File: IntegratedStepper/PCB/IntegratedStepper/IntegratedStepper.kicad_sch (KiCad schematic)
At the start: 0 parts

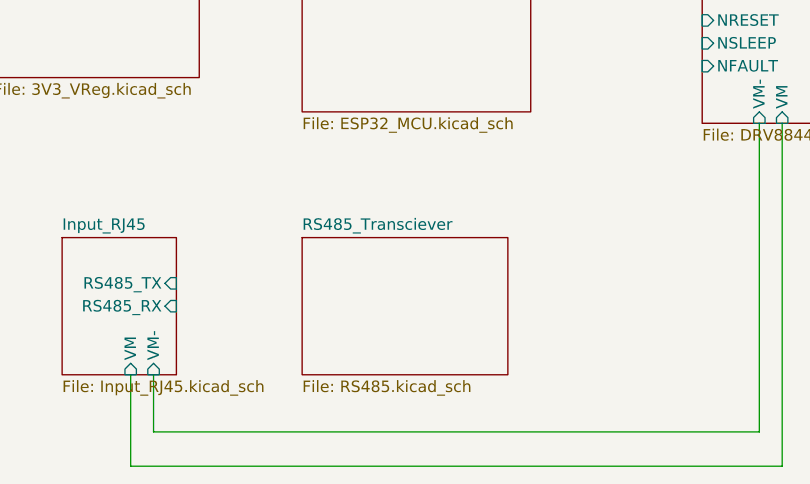
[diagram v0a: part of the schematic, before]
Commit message: Add CAN circuit and edit bus from RS485 to CAN
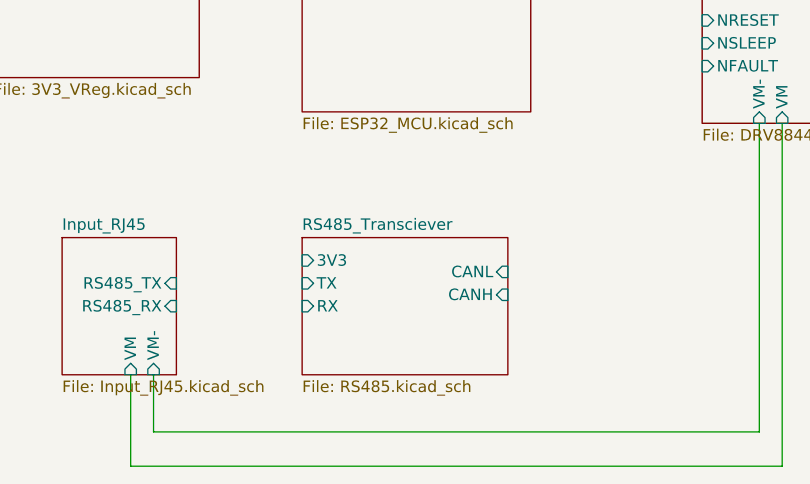
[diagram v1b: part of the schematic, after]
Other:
- sheet RS485_Transciever ports: added 3V3, CANH, CANL, RX, TX; removed none
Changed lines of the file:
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@@
       (effects (font (size 1.27 1.27)) (justify left top))
+    )
+    (pin "TX" input (at 104.14 111.76 180)
+      (effects (font (size 1.27 1.27)) (justify left))
+    )
+    (pin "RX" input (at 104.14 114.3 180)
+      (effects (font (size 1.27 1.27)) (justify left))
+    )
+    (pin "3V3" input (at 104.14 109.22 180)
+      (effects (font (size 1.27 1.27)) (justify left))
+    )
+    (pin "CANL" input (at 127 110.49 0)
+      (effects (font (size 1.27 1.27)) (justify right))
+    )
+    (pin "CANH" input (at 127 113.03 0)
+      (effects (font (size 1.27 1.27)) (justify right))
     )
     (instances

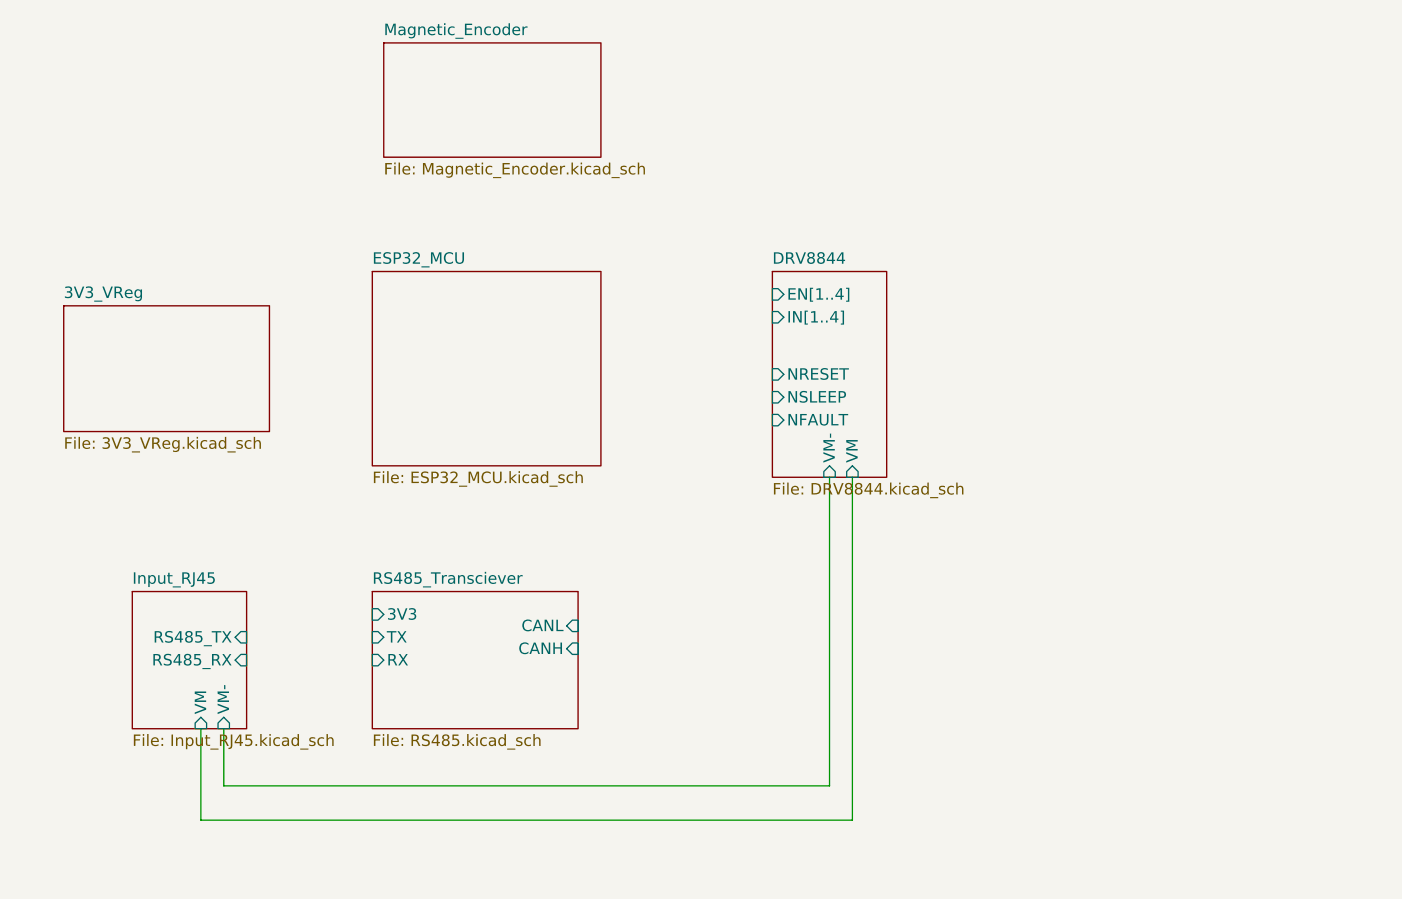
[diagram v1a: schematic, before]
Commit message: update Vreg for Integrated Stepper
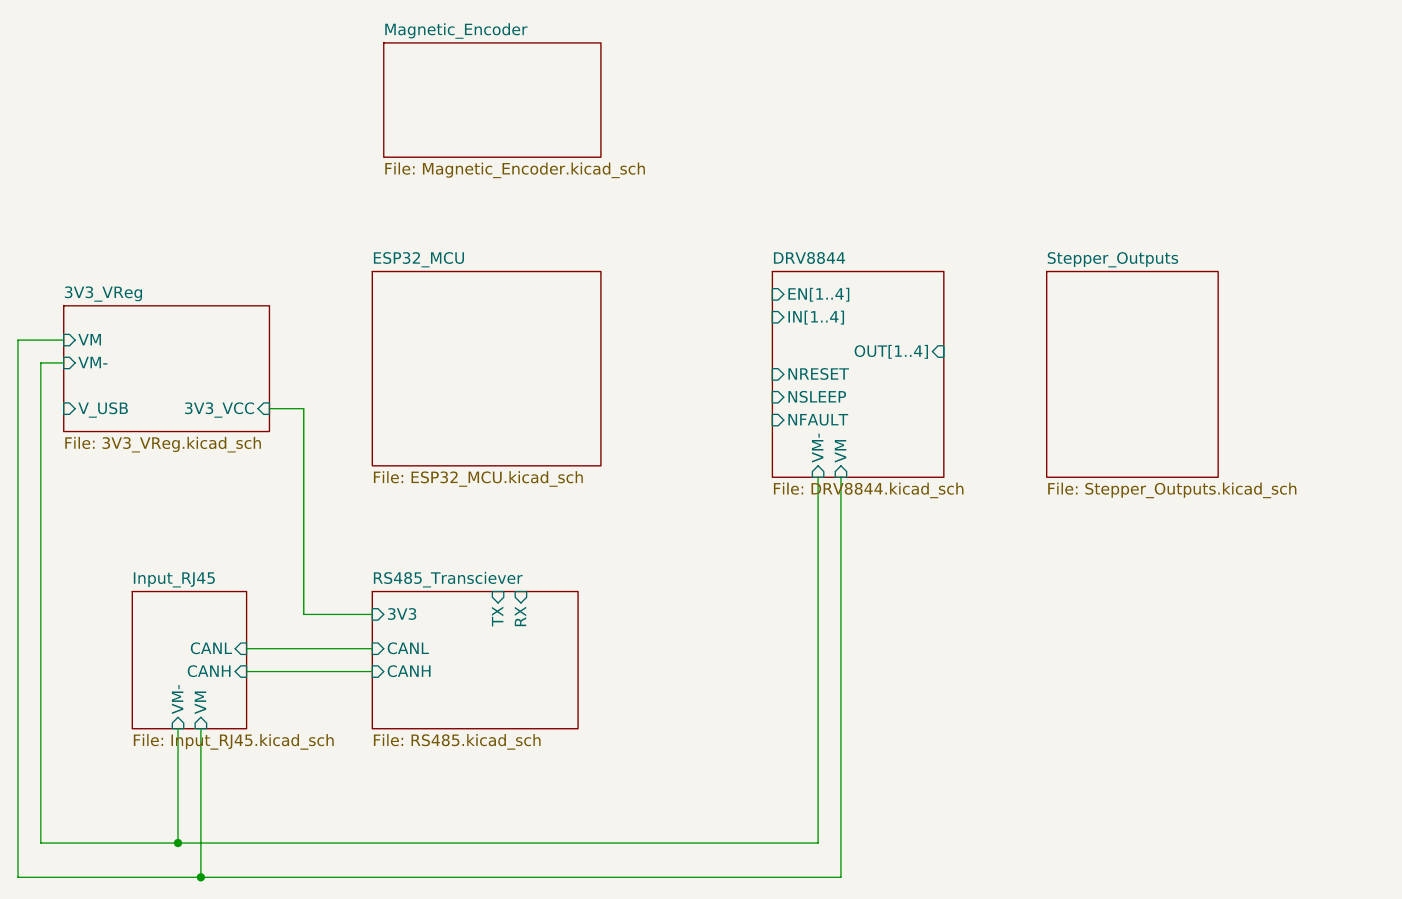
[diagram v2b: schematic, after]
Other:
- added sheet Stepper_Outputs (Stepper_Outputs.kicad_sch)
- sheet 3V3_VReg ports: added 3V3_VCC, VM, VM-, V_USB; removed none
- sheet DRV8844 ports: added OUT[1..4]; removed none
- sheet Input_RJ45 ports: added CANH, CANL; removed RS485_RX, RS485_TX
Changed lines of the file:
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@@
 (kicad_sch (version 20230121) (generator eeschema)
   (paper "A4")
-  (wire (pts (xy 87.63 121.92) (xy 87.63 128.27))
-    (stroke (width 0) (type default))
-  )
-  (wire (pts (xy 85.09 132.08) (xy 157.48 132.08))
-    (stroke (width 0) (type default))
-  )
-  (wire (pts (xy 87.63 128.27) (xy 154.94 128.27))
-    (stroke (width 0) (type default))
-  )
-  (wire (pts (xy 154.94 128.27) (xy 154.94 93.98))
-    (stroke (width 0) (type default))
-  )
-  (wire (pts (xy 85.09 121.92) (xy 85.09 132.08))
-    (stroke (width 0) (type default))
-  )
-  (wire (pts (xy 157.48 132.08) (xy 157.48 93.98))
+  (junction (at 85.09 138.43) (diameter 0) (color 0 0 0 0)
+  )
+  (junction (at 82.55 134.62) (diameter 0) (color 0 0 0 0)
+  )
+  (wire (pts (xy 82.55 121.92) (xy 82.55 134.62))
+    (stroke (width 0) (type default))
+  )
+  (wire (pts (xy 64.77 78.74) (xy 64.77 138.43))
+    (stroke (width 0) (type default))
+  )
+  (wire (pts (xy 96.52 86.36) (xy 96.52 109.22))
+    (stroke (width 0) (type default))
+  )
+  (wire (pts (xy 85.09 138.43) (xy 156.21 138.43))
+    (stroke (width 0) (type default))
+  )
+  (wire (pts (xy 92.71 86.36) (xy 96.52 86.36))
+    (stroke (width 0) (type default))
+  )
+  (wire (pts (xy 96.52 109.22) (xy 104.14 109.22))
+    (stroke (width 0) (type default))
+  )
+  (wire (pts (xy 82.55 134.62) (xy 153.67 134.62))
+    (stroke (width 0) (type default))
+  )
+  (wire (pts (xy 67.31 81.28) (xy 67.31 134.62))
+    (stroke (width 0) (type default))
+  )
+  (wire (pts (xy 90.17 115.57) (xy 104.14 115.57))
+    (stroke (width 0) (type default))
+  )
+  (wire (pts (xy 153.67 134.62) (xy 153.67 93.98))
+    (stroke (width 0) (type default))
+  )
+  (wire (pts (xy 64.77 138.43) (xy 85.09 138.43))
+    (stroke (width 0) (type default))
+  )
+  (wire (pts (xy 90.17 113.03) (xy 104.14 113.03))
+    (stroke (width 0) (type default))
+  )
+  (wire (pts (xy 85.09 121.92) (xy 85.09 138.43))
+    (stroke (width 0) (type default))
+  )
+  (wire (pts (xy 156.21 138.43) (xy 156.21 93.98))
+    (stroke (width 0) (type default))
+  )
+  (wire (pts (xy 69.85 81.28) (xy 67.31 81.28))
+    (stroke (width 0) (type default))
+  )
+  (wire (pts (xy 67.31 134.62) (xy 82.55 134.62))
+    (stroke (width 0) (type default))
+  )
+  (wire (pts (xy 69.85 78.74) (xy 64.77 78.74))
     (stroke (width 0) (type default))
   )
@@
       (effects (font (size 1.27 1.27)) (justify left))
     )
-    (pin "VM-" input (at 87.63 121.92 270)
-      (effects (font (size 1.27 1.27)) (justify left))
-    )
-    (pin "RS485_TX" input (at 90.17 111.76 0)
-      (effects (font (size 1.27 1.27)) (justify right))
-    )
-    (pin "RS485_RX" input (at 90.17 114.3 0)
+    (pin "VM-" input (at 82.55 121.92 270)
+      (effects (font (size 1.27 1.27)) (justify left))
+    )
+    (pin "CANL" input (at 90.17 113.03 0)
+      (effects (font (size 1.27 1.27)) (justify right))
+    )
+    (pin "CANH" input (at 90.17 115.57 0)
       (effects (font (size 1.27 1.27)) (justify right))
     )
@@
     )
   )
-  (sheet (at 148.59 71.12) (size 12.7 22.86) (fields_autoplaced)
+  (sheet (at 179.07 71.12) (size 19.05 22.86) (fields_autoplaced)
+    (stroke (width 0.1524) (type solid))
+    (fill (color 0 0 0 0.0000))
+    (property "Sheetname" "Stepper_Outputs" (at 179.07 70.4084 0)
+      (effects (font (size 1.27 1.27)) (justify left bottom))
+    )
+    (property "Sheetfile" "Stepper_Outputs.kicad_sch" (at 179.07 94.5646 0)
+      (effects (font (size 1.27 1.27)) (justify left top))
+    )
+    (instances
+      (project "IntegratedStepper"
+        (path "/ab592993-dafc-411a-b466-8e8425f43767" (page "8"))
+      )
+    )
+  )
+  (sheet (at 148.59 71.12) (size 19.05 22.86) (fields_autoplaced)
     (stroke (width 0.1524) (type solid))
     (fill (color 0 0 0 0.0000))
@@
       (effects (font (size 1.27 1.27)) (justify left top))
     )
-    (pin "VM-" input (at 154.94 93.98 270)
-      (effects (font (size 1.27 1.27)) (justify left))
-    )
-    (pin "VM" input (at 157.48 93.98 270)
+    (pin "VM-" input (at 153.67 93.98 270)
+      (effects (font (size 1.27 1.27)) (justify left))
+    )
+    (pin "VM" input (at 156.21 93.98 270)
       (effects (font (size 1.27 1.27)) (justify left))
     )
@@
       (effects (font (size 1.27 1.27)) (justify left))
     )
+    (pin "OUT[1..4]" input (at 167.64 80.01 0)
+      (effects (font (size 1.27 1.27)) (justify right))
+    )
     (instances
       (project "IntegratedStepper"
@@
       (effects (font (size 1.27 1.27)) (justify left top))
     )
+    (pin "3V3_VCC" input (at 92.71 86.36 0)
+      (effects (font (size 1.27 1.27)) (justify right))
+    )
+    (pin "V_USB" input (at 69.85 86.36 180)
+      (effects (font (size 1.27 1.27)) (justify left))
+    )
+    (pin "VM" input (at 69.85 78.74 180)
+      (effects (font (size 1.27 1.27)) (justify left))
+    )
+    (pin "VM-" input (at 69.85 81.28 180)
+      (effects (font (size 1.27 1.27)) (justify left))
+    )
     (instances
       (project "IntegratedStepper"
@@
       (effects (font (size 1.27 1.27)) (justify left top))
     )
-    (pin "TX" input (at 104.14 111.76 180)
-      (effects (font (size 1.27 1.27)) (justify left))
-    )
-    (pin "RX" input (at 104.14 114.3 180)
-      (effects (font (size 1.27 1.27)) (justify left))
+    (pin "TX" input (at 118.11 106.68 90)
+      (effects (font (size 1.27 1.27)) (justify right))
+    )
+    (pin "RX" input (at 120.65 106.68 90)
+      (effects (font (size 1.27 1.27)) (justify right))
     )
     (pin "3V3" input (at 104.14 109.22 180)
       (effects (font (size 1.27 1.27)) (justify left))
     )
-    (pin "CANL" input (at 127 110.49 0)
-      (effects (font (size 1.27 1.27)) (justify right))
-    )
-    (pin "CANH" input (at 127 113.03 0)
-      (effects (font (size 1.27 1.27)) (justify right))
-    )
-    (instances
+    (pin "CANL" input (at 104.14 113.03 180)
+      (effects (font (size 1.27 1.27)) (justify left))
+    )
+    (pin "CANH" input (at 104.14 115.57 180)
+      (effects (font (size 1.27 1.27)) (justify left))
+    )
+    (instances

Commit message: Update Integrated Stepper PCB with ESP sch and CAN sch
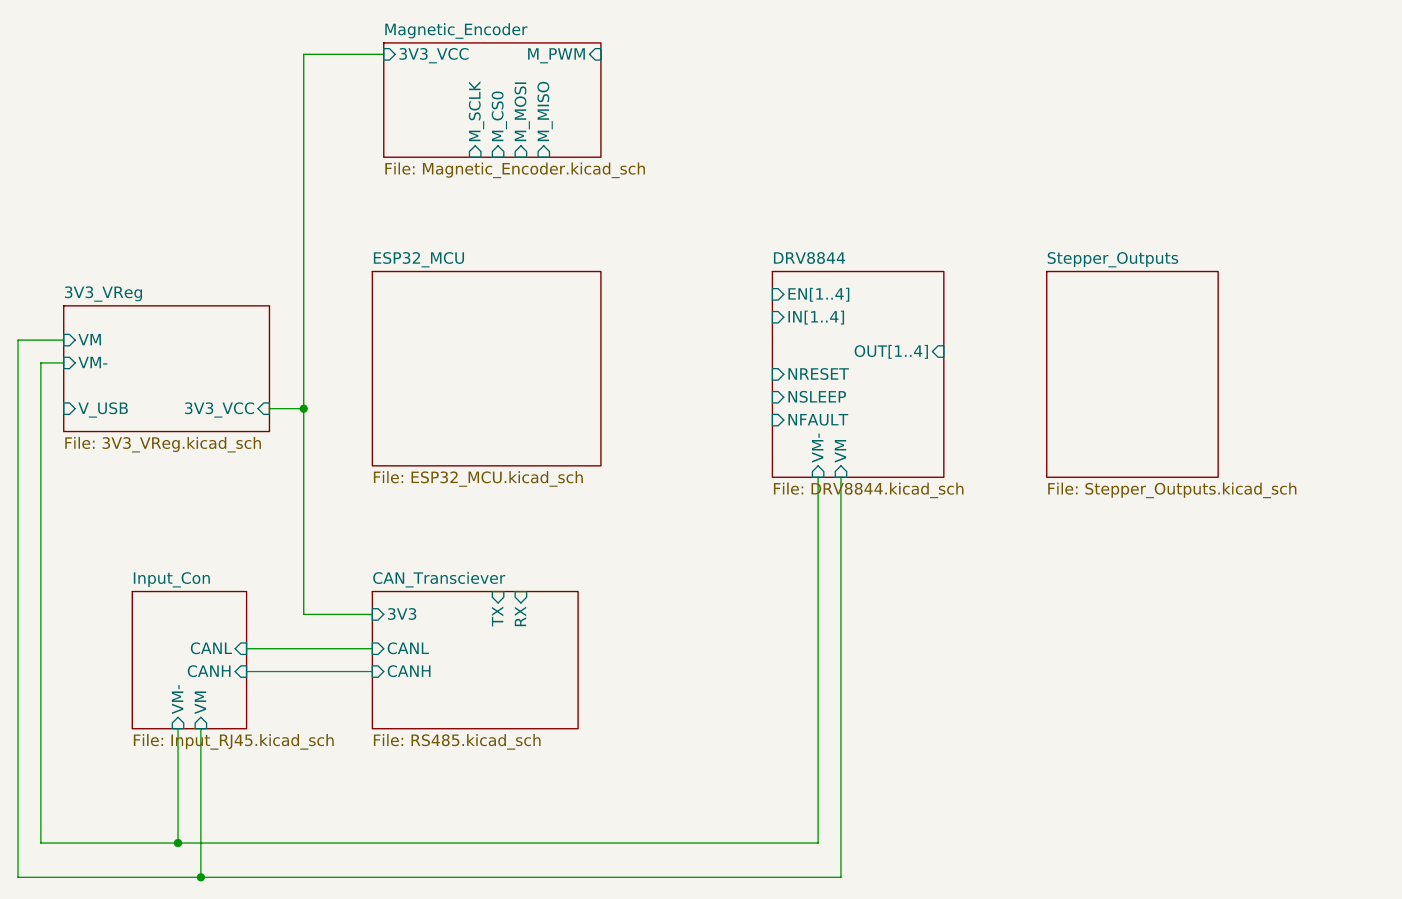
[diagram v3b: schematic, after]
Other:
- sheet Input_RJ45 renamed Input_Con
- sheet RS485_Transciever renamed CAN_Transciever
- sheet Magnetic_Encoder ports: added 3V3_VCC, M_CS0, M_MISO, M_MOSI, M_PWM, M_SCLK; removed none

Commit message: Update Integrated Stepper with inital PCB
This is going to be so hard :(
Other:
- sheet ESP32_MCU ports: added 3V3_VCC, CAN_RX, CAN_TX, ENC+, ENC-, ENC_IND, EN[1..4], I2C_SCL, I2C_SDA, IN[1..4], M_CS0, M_FAULT, M_MISO, M_MOSI, M_SCLK, USB_D+, USB_D-, VUSB; removed none
- sheet Input_Con ports: added ENC+, ENC-, ENC_IND, USB_D+, USB_D-, V_USB; removed none
- sheet Stepper_Outputs ports: added OUT[1..4]; removed none

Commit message: Add intermediate layout + routing to integrated stepper
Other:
- sheet CAN_Transciever ports: added CAN_RX, CAN_TX; removed RX, TX
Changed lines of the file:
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@@
-			)
-		)
-		(pin "TX" input
-			(at 129.54 111.76 90)
-			(effects
-				(font
-					(size 1.27 1.27)
-				)
-				(justify right)
-			)
-		)
-		(pin "RX" input
-			(at 132.08 111.76 90)
-			(effects
-				(font
-					(size 1.27 1.27)
-				)
-				(justify right)
 			)
 		)
@@
 			)
 		)
+		(pin "CAN_TX" input
+			(at 129.54 111.76 90)
+			(effects
+				(font
+					(size 1.27 1.27)
+				)
+				(justify right)
+			)
+		)
+		(pin "CAN_RX" input
+			(at 132.08 111.76 90)
+			(effects
+				(font
+					(size 1.27 1.27)
+				)
+				(justify right)
+			)
+		)

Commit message: add 3D model
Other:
- sheet Input_Con ports: added 3V3_VCC; removed none
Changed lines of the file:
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@@
-	)
-	(junction
-		(at 69.85 86.36)
-		(diameter 0)
-		(color 0 0 0 0)
 	)
 	(junction
@@
 		(color 0 0 0 0)
 	)
+	(junction
+		(at 68.58 86.36)
+		(diameter 0)
+		(color 0 0 0 0)
+	)
 	(wire
 		(pts
@@
 	(wire
 		(pts
-			(xy 69.85 74.93) (xy 69.85 86.36)
+			(xy 68.58 74.93) (xy 68.58 86.36)
 		)
 		(stroke
@@
 	(wire
 		(pts
+			(xy 69.85 96.52) (xy 69.85 106.68)
+		)
+		(stroke
+			(width 0)
+			(type default)
+		)
+	)
+	(wire
+		(pts
 			(xy 120.65 105.41) (xy 132.08 105.41)
 		)
@@
 	(wire
 		(pts
-			(xy 69.85 110.49) (xy 71.12 110.49)
+			(xy 68.58 113.03) (xy 71.12 113.03)
 		)
 		(stroke
@@
 	(wire
 		(pts
-			(xy 104.14 86.36) (xy 69.85 86.36)
-		)
-		(stroke
-			(width 0)
-			(type default)
-		)
-	)
-	(wire
-		(pts
 			(xy 104.14 74.93) (xy 96.52 74.93)
 		)
@@
 	(wire
 		(pts
-			(xy 69.85 86.36) (xy 69.85 110.49)
+			(xy 68.58 86.36) (xy 68.58 113.03)
 		)
 		(stroke
@@
 	(wire
 		(pts
+			(xy 68.58 86.36) (xy 104.14 86.36)
+		)
+		(stroke
+			(width 0)
+			(type default)
+		)
+	)
+	(wire
+		(pts
 			(xy 110.49 114.3) (xy 115.57 114.3)
 		)
@@
 		)
 	)
+	(wire
+		(pts
+			(xy 72.39 96.52) (xy 69.85 96.52)
+		)
+		(stroke
+			(width 0)
+			(type default)
+		)
+	)
 	(bus
 		(pts
@@
 	(wire
 		(pts
+			(xy 69.85 106.68) (xy 71.12 106.68)
+		)
+		(stroke
+			(width 0)
+			(type default)
+		)
+	)
+	(wire
+		(pts
 			(xy 64.77 138.43) (xy 77.47 138.43)
 		)
@@
 	(wire
 		(pts
-			(xy 71.12 74.93) (xy 69.85 74.93)
+			(xy 71.12 74.93) (xy 68.58 74.93)
 		)
 		(stroke
@@
 			(width 0)
 			(type default)
+		)
+	)
+	(global_label "3V3_VCC"
+		(shape input)
+		(at 72.39 96.52 0)
+		(fields_autoplaced yes)
+		(effects
+			(font
+				(size 1.27 1.27)
+			)
+			(justify left)
+		)
+		(property "Intersheetrefs" "${INTERSHEET_REFS}"
+			(at 83.479 96.52 0)
+			(effects
+				(font
+					(size 1.27 1.27)
+				)
+				(justify left)
+				(hide yes)
+			)
 		)
 	)
@@
 		)
 		(pin "V_USB" output
-			(at 71.12 110.49 180)
+			(at 71.12 113.03 180)
 			(effects
 				(font
@@
 			)
 		)
+		(pin "3V3_VCC" output
+			(at 71.12 106.68 180)
+			(effects
+				(font
+					(size 1.27 1.27)
+				)
+				(justify left)
+			)
+		)
